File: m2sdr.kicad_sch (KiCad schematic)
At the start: 71 parts, among them J1 Bus_M.2_Socket_B, J2 SMA, J3 SMA, P1 CONN_01X04, P2 CONN_01X01, P3 CONN_01X01, P4 CONN_01X01, P5 CONN_01X01, P6 CONN_01X01, P7 CONN_01X01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

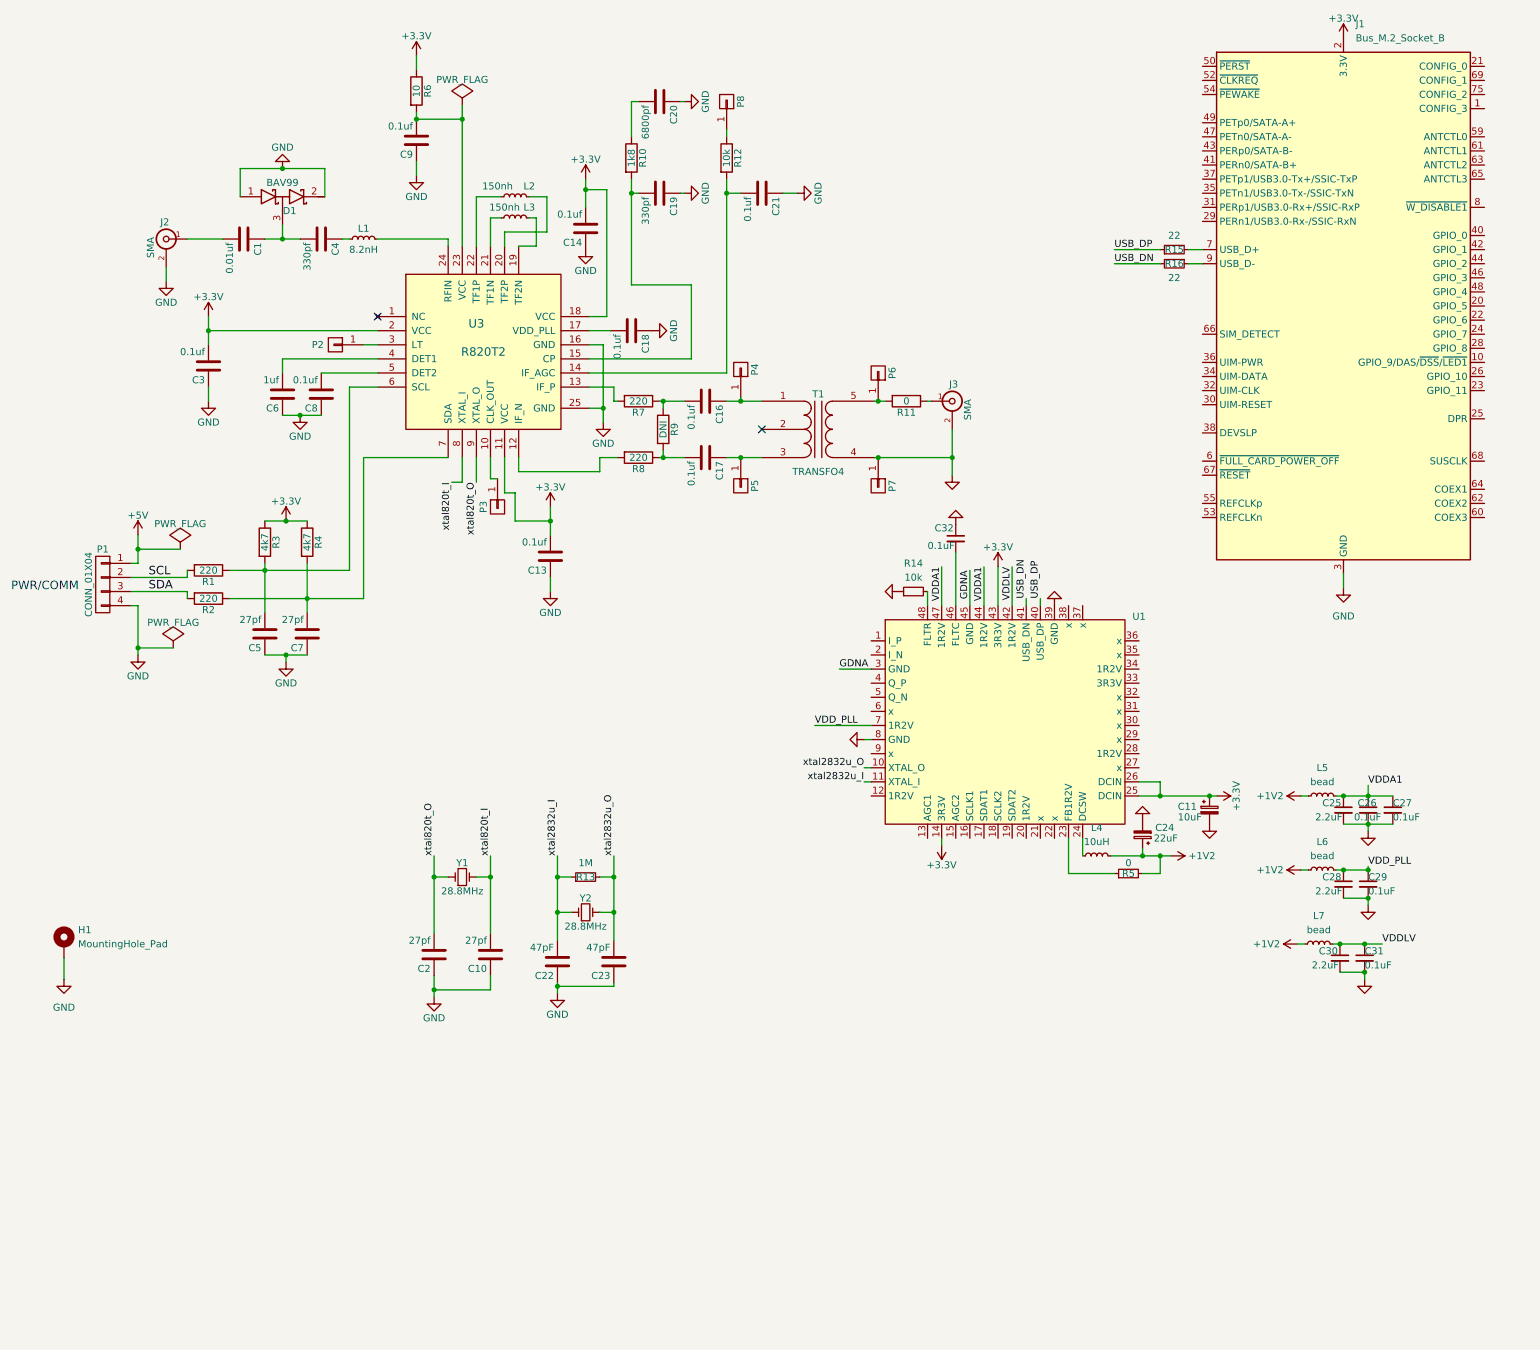
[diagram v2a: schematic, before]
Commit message: wired if_agc
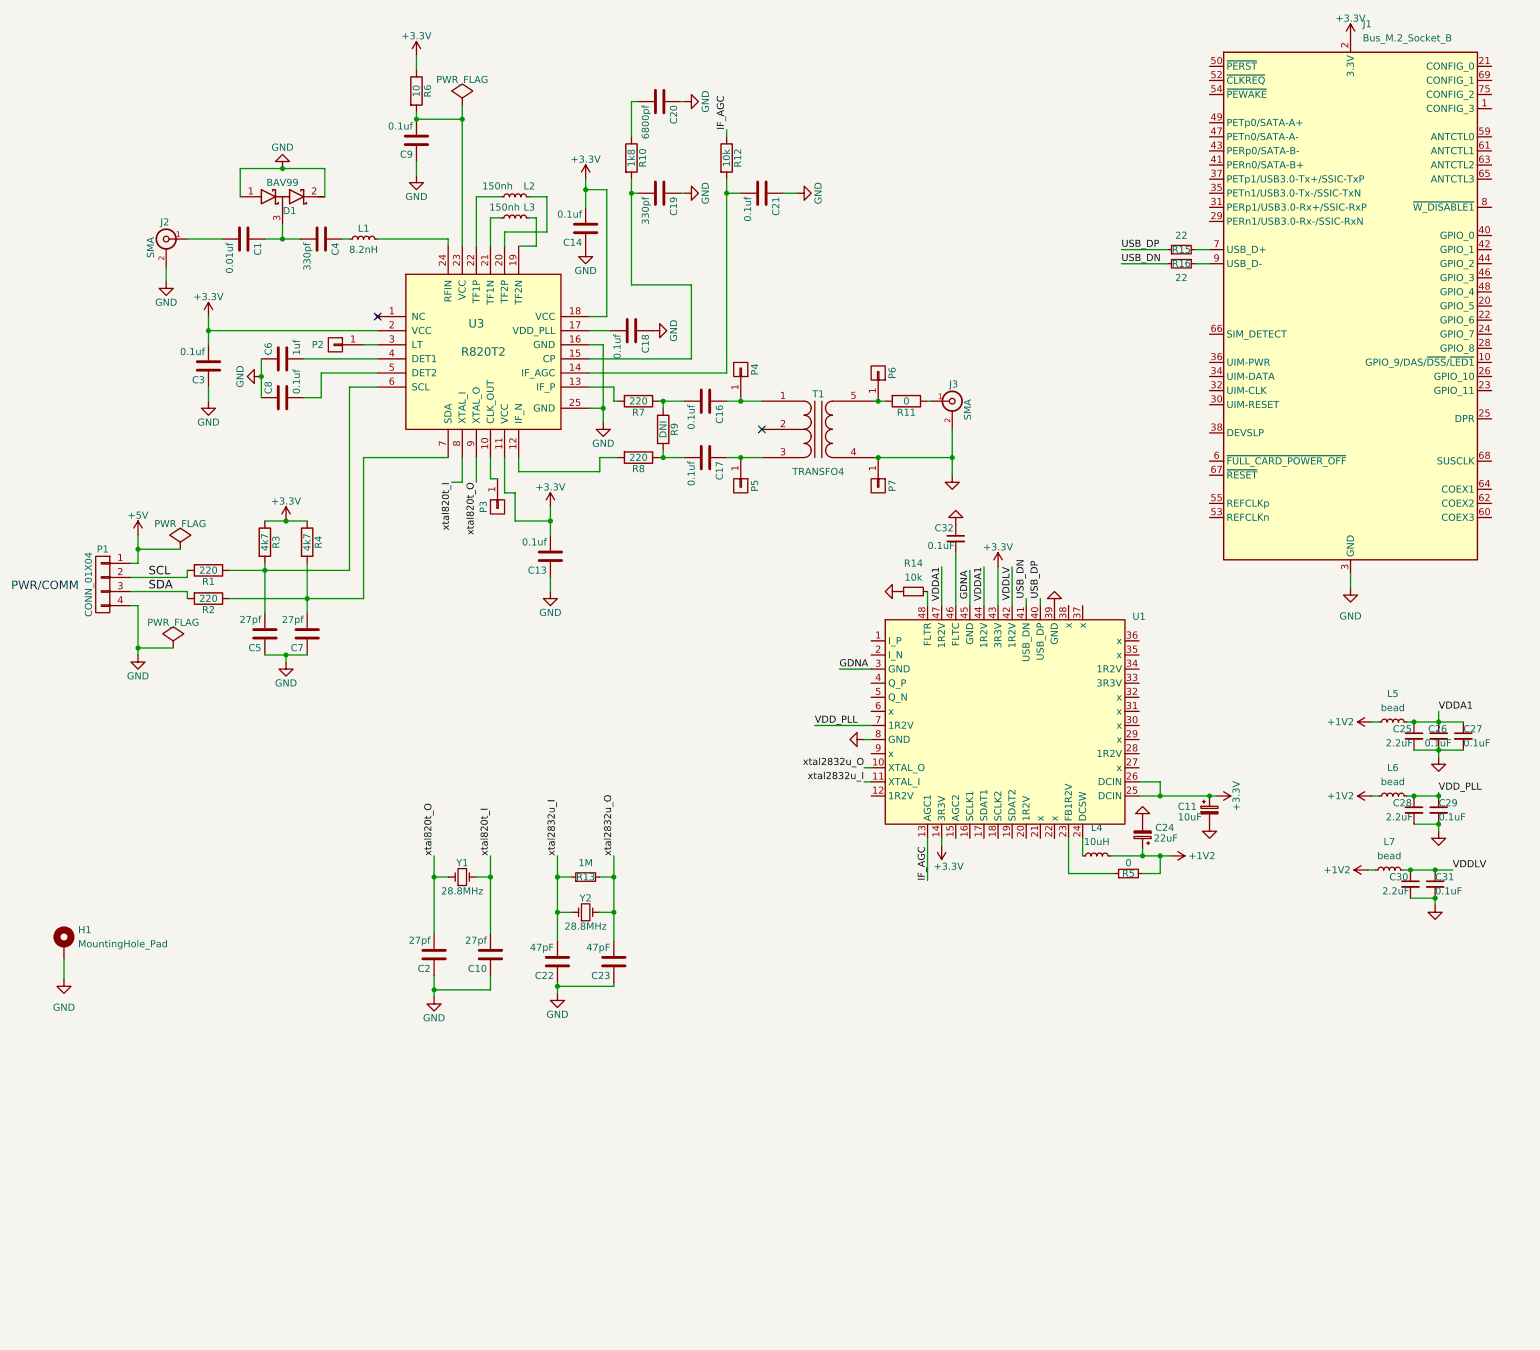
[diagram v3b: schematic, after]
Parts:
- removed P8: CONN_01X01, Connector_PinHeader_2.00mm:PinHeader_1x01_P2.00mm_Vertical, symbol r820t2_breakout-rescue:CONN_01X01
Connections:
- net IF_AGC: now reaches R12.1
- net IF_AGC: now also U1.13 (AGC1)
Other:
- moved on the sheet: C25, C26, C27, C28, C29, C30, C31, C6, C8, J1, L5, L6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
